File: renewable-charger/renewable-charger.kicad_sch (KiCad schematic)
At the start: 32 parts, among them J1 Solar Input, J2 Wind Output, J3 Output, M1 Stepper_Motor_bipolar, Q1 P-channel 30V 4A MOSfet, U1 CN3791

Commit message: Add test point to measure current into the battery.  Implements #8
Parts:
- added JP3: Test Point, Jumper:SolderJumper-2_P1.3mm_Bridged2Bar_RoundedPad1.0x1.5mm, symbol Jumper:SolderJumper_2_Bridged
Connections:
- net at C3.1, C7.1, J3.1 (Pin_1)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: now also JP3.1 (A); no longer BT1.1 (+)
- new net: BT1.1 (+), JP3.2 (B)
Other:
- moved on the sheet: BT1, C7

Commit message: Add micro-USB connector for USB charging.  Implements #7
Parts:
- added J?: USB_B_Micro, Connector_USB:USB_Micro-B_Amphenol_10118194_Horizontal, symbol Connector:USB_B_Micro
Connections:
- net Power +: now also J?.1 (VBUS)
- net Power -: now also J?.5 (GND)
- no-connect marks 0 -> 4
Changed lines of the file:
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@@
   (junction (at 57.15 132.08) (diameter 0) (color 0 0 0 0)
   )
+  (no_connect (at 29.21 154.94))
+  (no_connect (at 29.21 157.48))
+  (no_connect (at 29.21 160.02))
+  (no_connect (at 19.05 165.1))
   (wire (pts (xy 31.75 40.64) (xy 31.75 66.04))
     (stroke (width 0) (type default))
@@
     (stroke (width 0) (type default))
   )
+  (wire (pts (xy 21.59 165.1) (xy 21.59 167.64))
+    (stroke (width 0) (type default))
+  )
   (wire (pts (xy 73.66 76.2) (xy 92.71 76.2))
     (stroke (width 0) (type default))
@@
   )
   (wire (pts (xy 69.85 166.37) (xy 97.79 166.37))
+    (stroke (width 0) (type default))
+  )
+  (wire (pts (xy 29.21 149.86) (xy 31.75 149.86))
     (stroke (width 0) (type default))
   )
@@
     (effects (font (size 1.27 1.27)) (justify right))
   )
+  (hierarchical_label "Power -" (shape input) (at 21.59 167.64 270) (fields_autoplaced)
+    (effects (font (size 1.27 1.27)) (justify right))
+  )
+  (hierarchical_label "Power +" (shape input) (at 31.75 149.86 0) (fields_autoplaced)
+    (effects (font (size 1.27 1.27)) (justify left))
+  )
   (hierarchical_label "Power -" (shape input) (at 124.46 71.12 270) (fields_autoplaced)
     (effects (font (size 1.27 1.27)) (justify right))
@@
     (pin "1")
     (pin "2")
+  )
+  (symbol (lib_id "Connector:USB_B_Micro") (at 21.59 154.94 0) (unit 1)
+    (in_bom yes) (on_board yes) (fields_autoplaced)
+    (property "Reference" "J?" (id 0) (at 21.59 144.7546 0)
+      (effects (font (size 1.27 1.27)))
+    )
+    (property "Value" "USB_B_Micro" (id 1) (at 21.59 146.2786 0)
+      (effects (font (size 1.27 1.27)))
+    )
+    (property "Footprint" "Connector_USB:USB_Micro-B_Amphenol_10118194_Horizontal" (id 2) (at 25.4 156.21 0)
+      (effects (font (size 1.27 1.27)) hide)
+    )
+    (property "Datasheet" "~" (id 3) (at 25.4 156.21 0)
+      (effects (font (size 1.27 1.27)) hide)
+    )
+    (property "Farnell" "2668482" (id 4) (at 21.59 154.94 0)
+      (effects (font (size 1.27 1.27)) hide)
+    )
+    (property "Farnell Price/Stock" "https://uk.farnell.com/amphenol-icc-fci/10118194-0001lf/micro-usb-2-0-type-b-rcpt-smt/dp/2668482" (id 5) (at 21.59 154.94 0)
+      (effects (font (size 1.27 1.27)) hide)
+    )
+    (pin "1")
+    (pin "2")
+    (pin "3")
+    (pin "4")
+    (pin "5")
+    (pin "6")
   )
   (symbol (lib_id "Device:C_Polarized_Small") (at 92.71 44.45 0) (unit 1)
@@
       (reference "J3") (unit 1) (value "Output") (footprint "Connector_Phoenix_MSTB:PhoenixContact_MSTBVA_2,5_2-G-5,08_1x02_P5.08mm_Vertical")
     )
+    (path "/0ac0d458-acb2-4d0a-9919-5b8c48cac303"
+      (reference "J?") (unit 1) (value "USB_B_Micro") (footprint "Connector_USB:USB_Micro-B_Amphenol_10118194_Horizontal")
+    )
     (path "/83d8a3bf-88d6-4c2b-bba9-61242c32e20a"

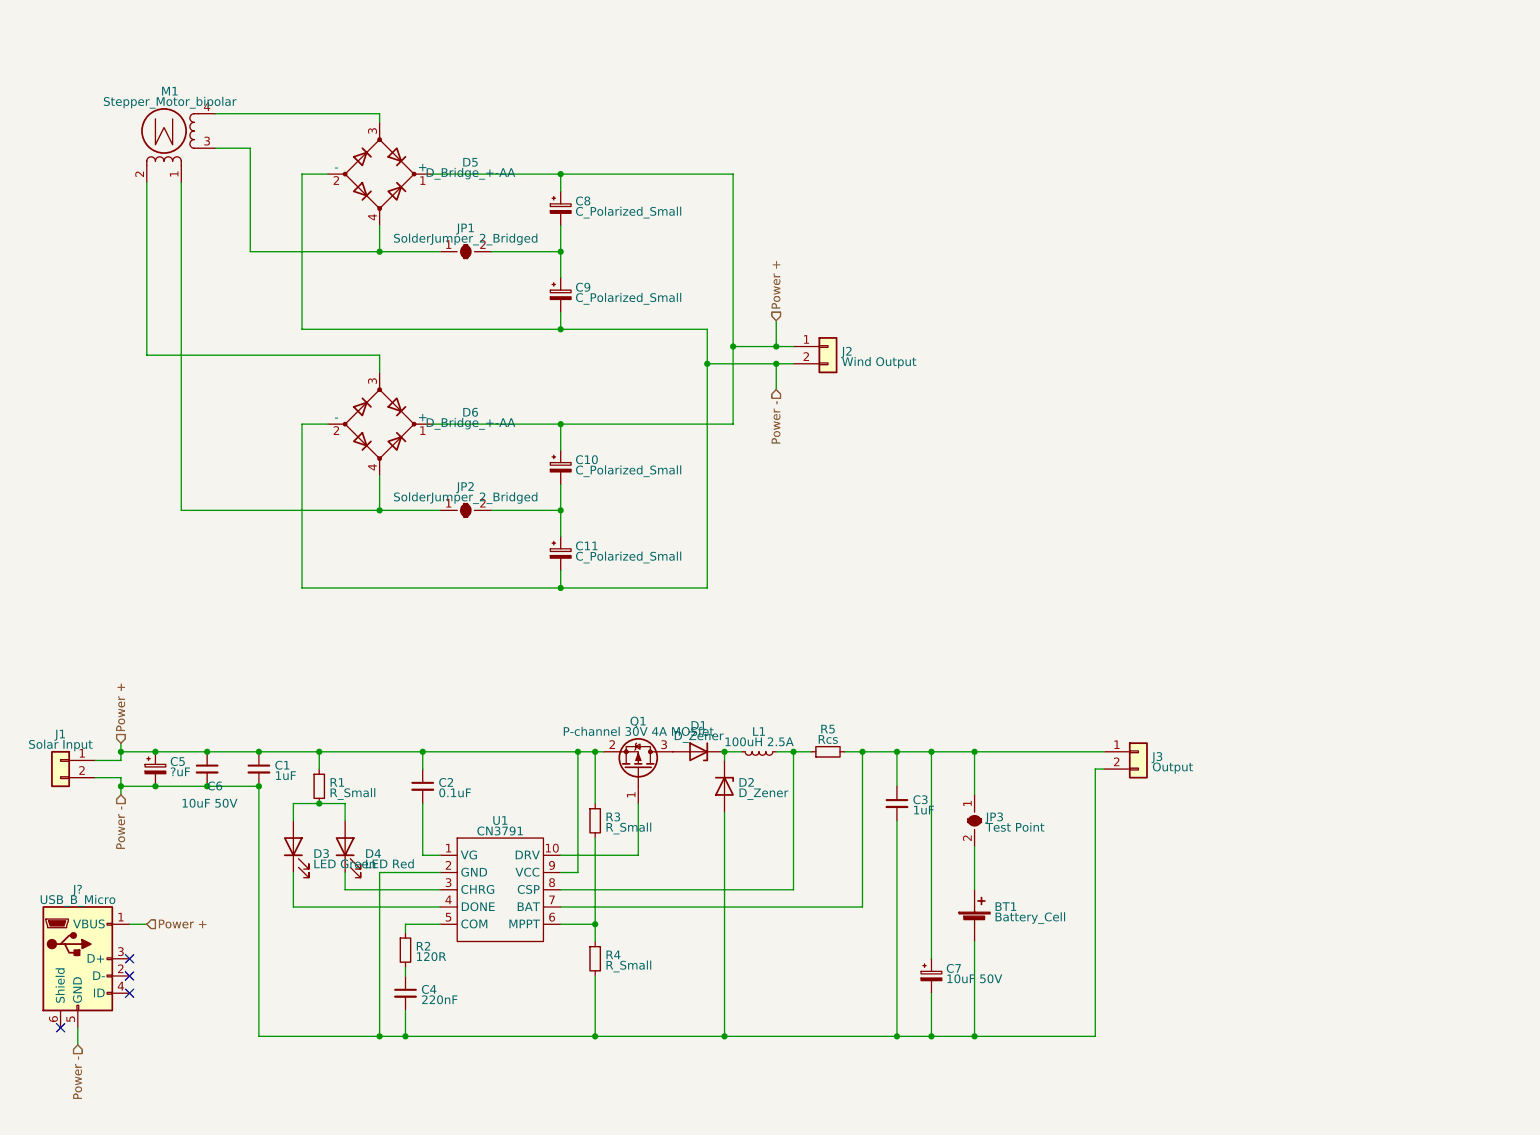
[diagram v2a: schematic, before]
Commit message: Disconnect battery output when charging; add through-hole battery connector alternative.  Part of #5
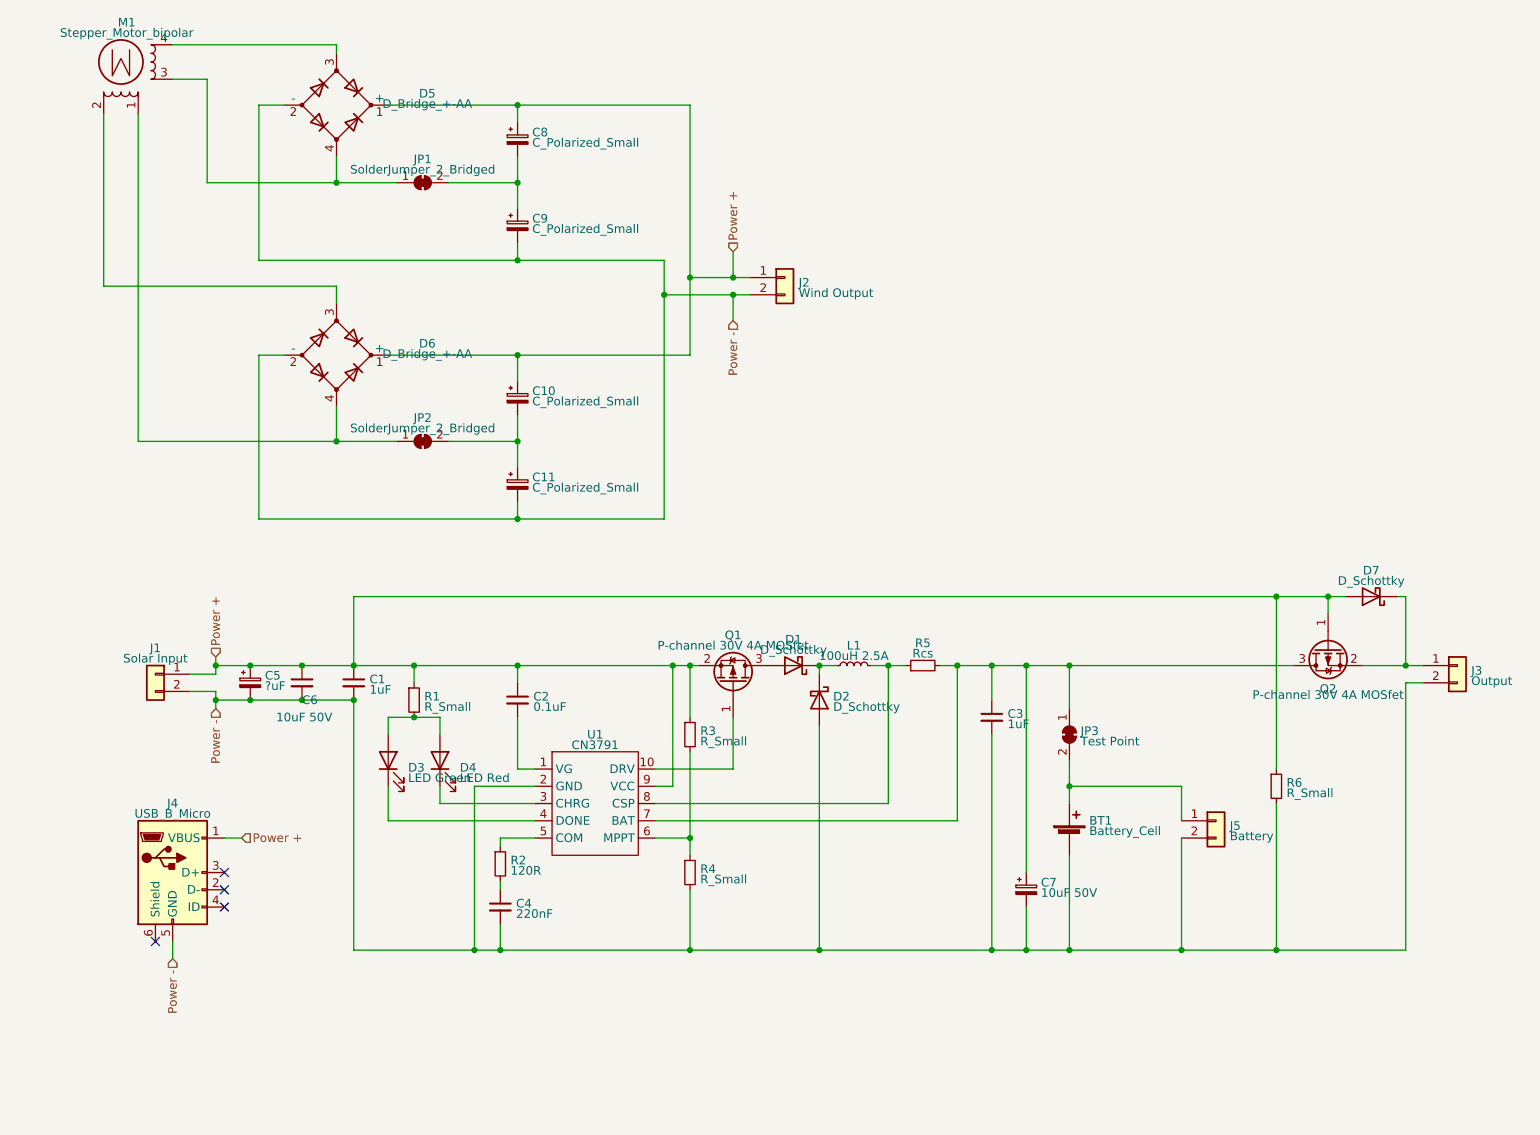
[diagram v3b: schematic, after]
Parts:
- added D7: D_Schottky, Diode_SMD:D_SMF, symbol Device:D_Schottky
- added J5: Battery, Connector_PinHeader_2.54mm:PinHeader_1x02_P2.54mm_Vertical, symbol Connector_Generic:Conn_01x02
- added Q2: P-channel 30V 4A MOSfet, Package_TO_SOT_SMD:SOT-23, symbol Transistor_FET:AO3401A
- added R6: R_Small, Resistor_SMD:R_0603_1608Metric_Pad0.98x0.95mm_HandSolder, symbol Device:R_Small
- D1, D2: value D_Zener -> D_Schottky; symbol Device:D_Zener -> Device:D_Schottky
- gave numbers to parts that had none: 1
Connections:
- net Power +: now also D7.2 (A), Q2.1 (G), R6.1
- net Power -: now also J5.2 (Pin_2), R6.2
- net at C3.1, C7.1, JP3.1 (A)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: now also Q2.3 (D); no longer J3.1 (Pin_1)
- net at BT1.1 (+), JP3.2 (B): now also J5.1 (Pin_1)
- new net: D7.1 (K), J3.1 (Pin_1), Q2.2 (S)
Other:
- moved on the sheet: BT1, C1, C10, C11, C2, C3, C4, C5, C6, C7, C8, C9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

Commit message: All connections wired on PCB.  Still needs zones, final position for mounting holes and edges, and some labelling.  Part of #4
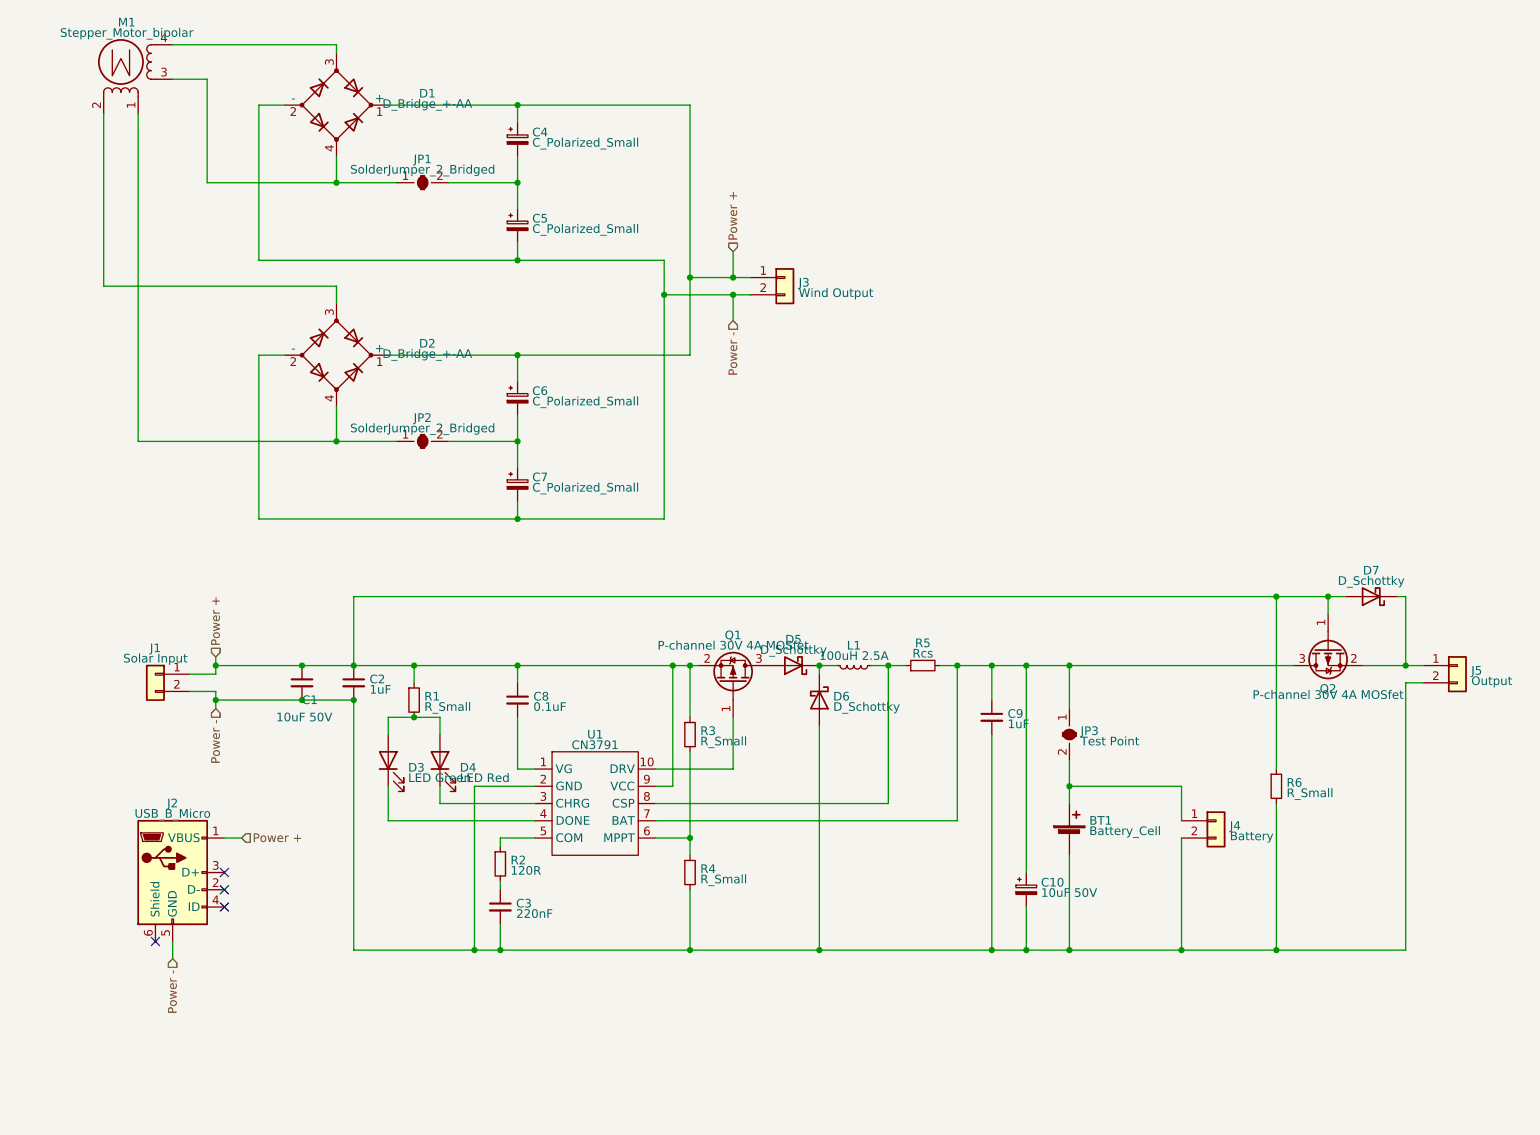
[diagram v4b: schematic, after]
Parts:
- removed C5: ?uF, symbol Device:C_Polarized_Small
- renumbered C6 to C1, C7 to C10, C1 to C2, C4 to C3, C8 to C4, C9 to C5, C10 to C6, C11 to C7, C2 to C8, C3 to C9, D5 to D1, D6 to D2, D1 to D5, D2 to D6, J4 to J2, J2 to J3, J5 to J4, J3 to J5
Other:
- moved on the sheet: L1
